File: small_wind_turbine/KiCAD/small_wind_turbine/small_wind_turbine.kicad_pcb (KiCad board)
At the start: 2 copper layers, 90 x 90 mm, 94 parts, among them J1 Conn_01x03_Male, J2 Conn_01x03_Male, J3 Conn_01x03_Male, K1 G5LE-1, Q1 Q_NMOS_GDS, SW1 SW_Push_SPDT, U10 AZ1117-5.0, U2 UC2844A, U3 LTC4440ES6, U4 Opamp_Quad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

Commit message: tweak aesthetics
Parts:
- moved D12 0.40 mm to (105.1, 34.9)
- moved R18 0.40 mm to (100.9, 34.9)
- renumbered G2 to Gen, G1 to JEH
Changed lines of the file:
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@@
   )
   (footprint "LED_SMD:LED_0603_1608Metric" (layer "F.Cu")
-    (at 105.4875 34.9 180)
+    (at 105.0875 34.9 180)
     (descr "LED SMD 0603 (1608 Metric), square (rectangular) end terminal, IPC_7351 nominal, (Body size source: http://www.tortai-tech.com/upload/download/2011102023233369053.pdf), generated with kicad-footprint-generator")
     (tags "LED")
@@
     (at 108 101.2)
     (attr board_only exclude_from_pos_files exclude_from_bom)
-    (fp_text reference "G1" (at -63.5 18.085) (layer "F.SilkS")
+    (fp_text reference "JEH" (at -0.2 16) (layer "F.SilkS")
       (effects (font (size 1.524 1.524) (thickness 0.3)))
     )
@@
   )
   (footprint "Resistor_SMD:R_0805_2012Metric" (layer "F.Cu")
-    (at 101.2875 34.9)
+    (at 100.8875 34.9)
     (descr "Resistor SMD 0805 (2012 Metric), square (rectangular) end terminal, IPC_7351 nominal, (Body size source: IPC-SM-782 page 72, https://www.pcb-3d.com/wordpress/wp-content/uploads/ipc-sm-782a_amendment_1_and_2.pdf), generated with kicad-footprint-generator")
     (tags "resistor")
@@
     (property "Sheetname" "")
     (attr through_hole)
-    (fp_text reference "F1" (at -9.225 -5.835) (layer "F.SilkS")
+    (fp_text reference "F1" (at 0 -5.8) (layer "F.SilkS")
       (effects (font (size 1 1) (thickness 0.15)))
     )
@@
     (property "Sheetname" "")
     (attr through_hole)
-    (fp_text reference "Jres1" (at 0.105 -11.889 -90) (layer "F.SilkS")
+    (fp_text reference "Jres1" (at 2.7 -8.2 -90) (layer "F.SilkS")
       (effects (font (size 1.4 1.4) (thickness 0.15)))
     )
@@
     (at 80.962546 78.042611 180)
     (attr board_only exclude_from_pos_files exclude_from_bom)
-    (fp_text reference "G2" (at 36.462546 -41.407389) (layer "B.SilkS")
+    (fp_text reference "Gen" (at -43.937454 -19.257389) (layer "B.SilkS")
       (effects (font (size 1.524 1.524) (thickness 0.3)) (justify mirror))
     )
@@
   (segment (start 78.1 81.8) (end 78.121 81.779) (width 0.508) (layer "F.Cu") (net 4))
   (segment (start 52.62 92.7) (end 53.7825 92.7) (width 0.508) (layer "F.Cu") (net 4))
-  (segment (start 106.275 34.9) (end 107.7 34.9) (width 0.2) (layer "F.Cu") (net 4))
+  (segment (start 105.875 34.9) (end 107.3 34.9) (width 0.2) (layer "F.Cu") (net 4))
   (segment (start 49.15 74.1) (end 47.8 72.75) (width 0.508) (layer "F.Cu") (net 4))
   (segment (start 122.2125 34.9) (end 120.8 34.9) (width 0.2) (layer "F.Cu") (net 4))
@@
   (via (at 65.126 83.9) (size 1.524) (drill 1.016) (layers "F.Cu" "B.Cu") (net 4))
   (via (at 125.2 78.1) (size 0.508) (drill 0.3302) (layers "F.Cu" "B.Cu") (net 4))
-  (via (at 107.7 34.9) (size 0.508) (drill 0.3302) (layers "F.Cu" "B.Cu") (net 4))
+  (via (at 107.3 34.9) (size 0.508) (drill 0.3302) (layers "F.Cu" "B.Cu") (net 4))
   (via (at 55.8 78.2) (size 0.508) (drill 0.3302) (layers "F.Cu" "B.Cu") (net 4))
   (via (at 55.1 86.4) (size 1.524) (drill 1.016) (layers "F.Cu" "B.Cu") (net 4))
@@
   (via (at 68.1 75.1) (size 0.508) (drill 0.3302) (layers "F.Cu" "B.Cu") (net 4))
   (via (at 120.8 34.9) (size 0.508) (drill 0.3302) (layers "F.Cu" "B.Cu") (net 4))
-  (segment (start 70 89.2) (end 68.7 87.9) (width 0.2) (layer "F.Cu") (net 5))
   (segment (start 78.3875 97.585) (end 78.49 97.585) (width 0.2) (layer "F.Cu") (net 5))
-  (segment (start 71.4 90.6) (end 71.4025 90.6) (width 0.2) (layer "F.Cu") (net 5))
+  (segment (start 69.558616 89.658616) (end 67.8 87.9) (width 0.2) (layer "F.Cu") (net 5))
   (segment (start 65.6 87.9) (end 62.9 85.2) (width 0.2) (layer "F.Cu") (net 5))
-  (segment (start 68.7 87.9) (end 65.6 87.9) (width 0.2) (layer "F.Cu") (net 5))
-  (segment (start 71.4025 90.6) (end 78.3875 97.585) (width 0.2) (layer "F.Cu") (net 5))
-  (via (at 70 89.2) (size 0.508) (drill 0.3302) (layers "F.Cu" "B.Cu") (net 5))
-  (via (at 71.4 90.6) (size 0.508) (drill 0.3302) (layers "F.Cu" "B.Cu") (net 5))
-  (segment (start 70 89.2) (end 71.4 90.6) (width 0.2) (layer "B.Cu") (net 5))
-  (segment (start 71.2 85.5) (end 71.2 82.08) (width 0.2) (layer "F.Cu") (net 6))
-  (segment (start 72.159866 92.140134) (end 72.159866 93.359866) (width 0.2) (layer "F.Cu") (net 6))
-  (segment (start 72.159866 93.359866) (end 75.95 97.15) (width 0.2) (layer "F.Cu") (net 6))
+  (segment (start 67.8 87.9) (end 65.6 87.9) (width 0.2) (layer "F.Cu") (net 5))
+  (segment (start 73.7025 92.9) (end 78.3875 97.585) (width 0.2) (layer "F.Cu") (net 5))
+  (segment (start 72.8 92.9) (end 73.7025 92.9) (width 0.2) (layer "F.Cu") (net 5))
+  (via (at 69.558616 89.658616) (size 0.508) (drill 0.3302) (layers "F.Cu" "B.Cu") (net 5))
+  (via (at 72.8 92.9) (size 0.508) (drill 0.3302) (layers "F.Cu" "B.Cu") (net 5))
+  (segment (start 72.8 92.9) (end 69.558616 89.658616) (width 0.2) (layer "B.Cu") (net 5))
   (segment (start 75.95 97.15) (end 75.95 97.585) (width 0.2) (layer "F.Cu") (net 6))
-  (via (at 72.159866 92.140134) (size 0.508) (drill 0.3302) (layers "F.Cu" "B.Cu") (net 6))
+  (segment (start 71.2 85.5) (end 71.2 82.08) (width 0.2) (layer "F.Cu") (net 6))
+  (segment (start 72.2 93.4) (end 75.95 97.15) (width 0.2) (layer "F.Cu") (net 6))
+  (segment (start 72.2 89.6) (end 72.2 93.4) (width 0.2) (layer "F.Cu") (net 6))
+  (via (at 72.2 89.6) (size 0.508) (drill 0.3302) (layers "F.Cu" "B.Cu") (net 6))
   (via (at 71.2 85.5) (size 0.508) (drill 0.3302) (layers "F.Cu" "B.Cu") (net 6))
-  (segment (start 72.2 92.1) (end 72.2 89.016525) (width 0.2) (layer "B.Cu") (net 6))
-  (segment (start 72.159866 92.140134) (end 72.2 92.1) (width 0.2) (layer "B.Cu") (net 6))
+  (segment (start 72.2 89.6) (end 72.2 89.016525) (width 0.2) (layer "B.Cu") (net 6))
   (segment (start 71.2 88.016525) (end 71.2 85.5) (width 0.2) (layer "B.Cu") (net 6))
   (segment (start 72.2 89.016525) (end 71.2 88.016525) (width 0.2) (layer "B.Cu") (net 6))
@@
   (segment (start 119.3125 81.1) (end 121.6125 81.1) (width 0.2) (layer "F.Cu") (net 43))
   (segment (start 119.3125 84.1) (end 121.6125 84.1) (width 0.2) (layer "F.Cu") (net 44))
-  (segment (start 104.7 34.9) (end 102.2 34.9) (width 0.2) (layer "F.Cu") (net 45))
+  (segment (start 104.3 34.9) (end 101.8 34.9) (width 0.2) (layer "F.Cu") (net 45))
   (segment (start 103.455 45.535) (end 99.92 42) (width 0.508) (layer "F.Cu") (net 46))
   (segment (start 106 45.535) (end 103.455 45.535) (width 0.508) (layer "F.Cu") (net 46))
-  (segment (start 99.92 35.355) (end 99.92 42) (width 0.2) (layer "F.Cu") (net 46))
-  (segment (start 100.375 34.9) (end 99.92 35.355) (width 0.2) (layer "F.Cu") (net 46))
+  (segment (start 99.92 42) (end 99.92 34.955) (width 0.2) (layer "F.Cu") (net 46))
+  (segment (start 99.92 34.955) (end 99.975 34.9) (width 0.2) (layer "F.Cu") (net 46))
   (segment (start 57.9825 85.3625) (end 57.82 85.2) (width 0.508) (layer "F.Cu") (net 47))
   (segment (start 57.9825 87.95) (end 57.9825 85.3625) (width 0.508) (layer "F.Cu") (net 47))

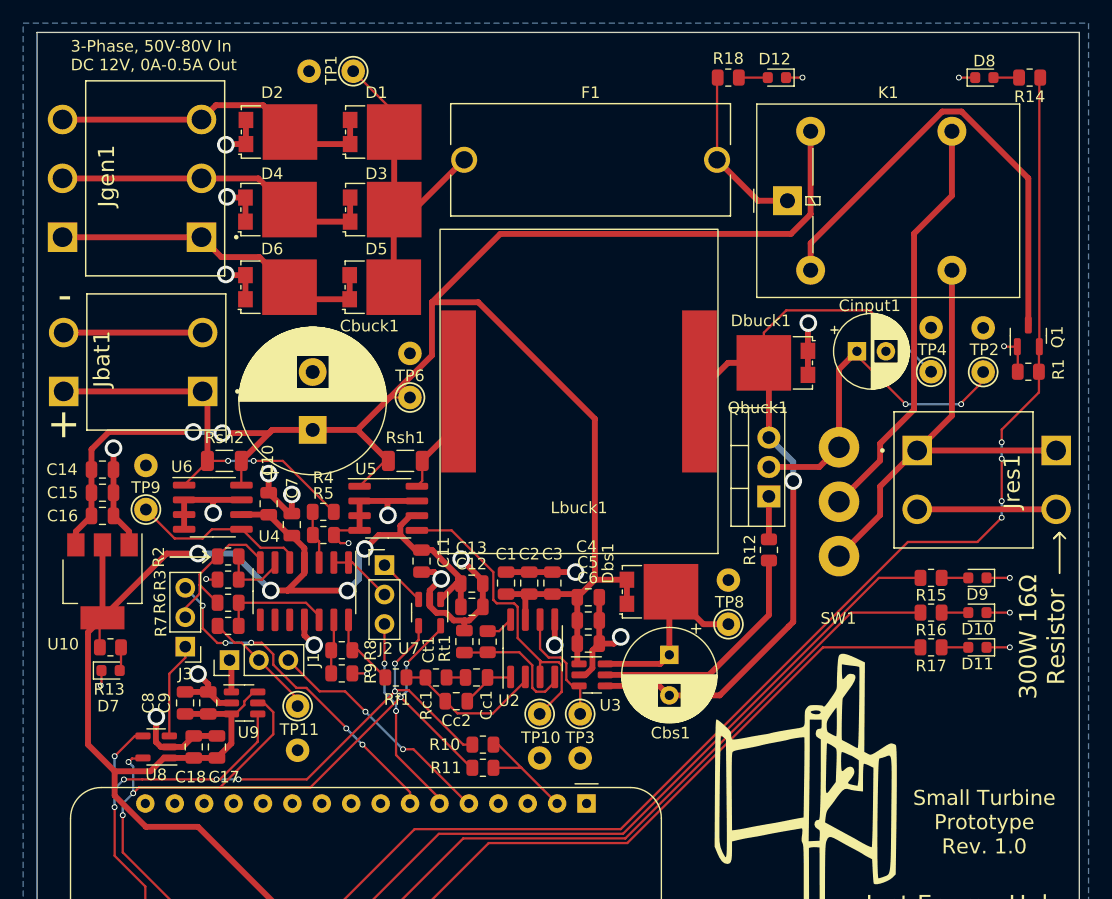
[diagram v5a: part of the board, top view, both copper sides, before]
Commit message: add jumper to switch 5V rail
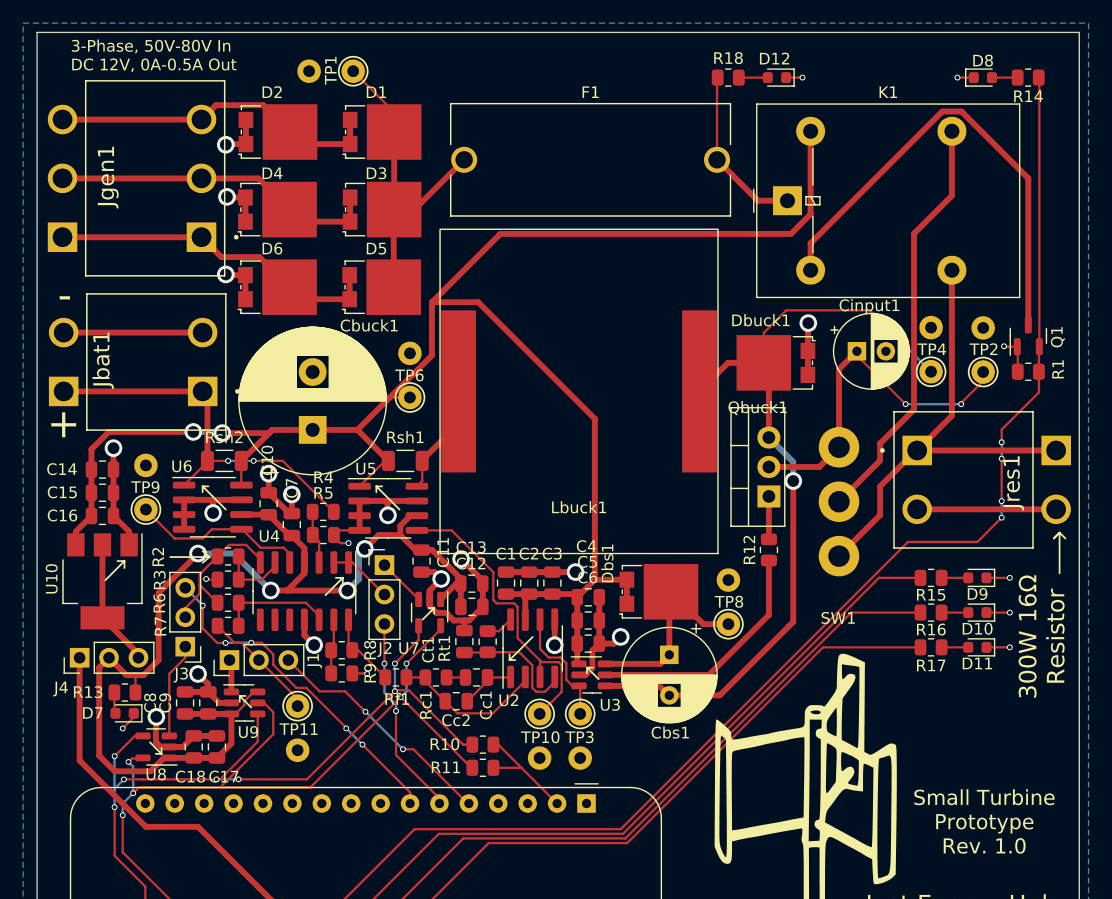
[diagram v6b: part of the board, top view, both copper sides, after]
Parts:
- added J4: Conn_01x03_Male, Connector_PinHeader_2.54mm:PinHeader_1x03_P2.54mm_Vertical, F.Cu at (44.9, 85.0)
- moved R13 4.10 mm to (48.8, 88.0), turned to 180 degrees
- moved D7 3.89 mm to (48.8, 89.8), turned to 180 degrees
- moved D8 0.12 mm to (122.9, 34.9)
- moved R14 0.12 mm to (126.8, 34.9)
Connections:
- A1 pad 26: +5V -> Net-(A1-Pad26)
- U10 pad 2: +5V -> Net-(U10-Pad2)
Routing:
- net Net-(A1-Pad26): track 0.00 -> 47.4 mm
- net +5V: track 138.4 -> 96.1 mm
- net Net-(U10-Pad2): track 0.00 -> 11.0 mm
